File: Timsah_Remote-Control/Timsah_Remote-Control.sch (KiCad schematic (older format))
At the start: 41 parts, among them J1 Güç Girişi, J2 ICSP, J3 Klemens, SW1 Oto Depth, SW10 Backward, SW2 Lights, SW3 Up, SW4 Down, SW5 Power, SW6 Turn Back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

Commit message: Remote control board recreated.
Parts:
- added D2: LED, LED_THT:LED_D5.0mm, symbol Device:LED
- added R18: 1k, Resistor_THT:R_Axial_DIN0207_L6.3mm_D2.5mm_P10.16mm_Horizontal, symbol Device:R
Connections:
- net +5V: now also R4.1
- net Down: now also U3.10 (RE2/CCP5/AN7); no longer U3.28 (RD5/P1B/AN25)
- net ENABLE: now also U3.36 (AN9/C12IN2-/CTED2/CCP2/RB3); no longer U3.2 (AN0/C12IN0-/RA0)
- net Forward: now also U3.23 (RC4/SDA1/SDI1/AN16); no longer U3.19 (RD0/SCL2/SCK2/AN20)
- net GND: now also R18.1; no longer R4.1
- net OTO_DEPTH: now also U3.4 (DACOUT/VREF-/AN2/C2IN+/RA2); no longer U3.30 (RD7/RX2/DT2/P1D/AN27)
- net Right: now also U3.24 (RC5/SDO1/AN17); no longer U3.20 (RD1/SDI1/SDA2/CCP4/AN21)
- net SERVO_Cam: now also U3.20 (RD1/SDI1/SDA2/CCP4/AN21); no longer U3.17 (RC2/CTPLS/CCP1/P1A/T5CKI/AN14)
- net SERVO_Grip: now also U3.35 (AN8/CTED1/INT2/RB2); no longer U3.18 (RC3/SCL1/SCK1/AN15)
- net TURN_BACK: now also U3.18 (RC3/SCL1/SCK1/AN15); no longer U3.29 (RD6/TX2/CK2/P1C/AN26)
- net Up: now also U3.9 (RE1/P3B/AN6); no longer U3.27 (RD4/P2D/SDO2/AN24)
- net VRX-A: now also U3.15 (RC0/P2B/SOSCO/T1CKI/T3CKI/T3G); no longer U3.33 (AN12/SRI/FLT0/INT0/RB0)
- net VRX-B: now also U3.37 (AN11/T5G/IOC/RB4); no longer U3.35 (AN8/CTED1/INT2/RB2)
- net VRY-A: now also U3.16 (RC1/SOSCI/P2A/CCP2); no longer U3.34 (AN10/C12IN3-/INT1/RB1)
- net VRY-B: now also U3.38 (AN13/CCP3/T1G/IOC/CCP3/RB5); no longer U3.36 (AN9/C12IN2-/CTED2/CCP2/RB3)
- new net: D2.1 (K), R18.2
- new net LED: D2.2 (A), U3.17 (RC2/CTPLS/CCP1/P1A/T5CKI/AN14)
- no-connect marks 18 -> 17
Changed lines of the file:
@@
 Wire Wire Line
 	6950 950  6950 1050
-Text GLabel 1300 2650 0    50   Input ~ 0
+Text GLabel 1300 1650 0    50   Input ~ 0
 SERVO_Cam
 Text Notes 7000 2100 0    79   ~ 16
@@
 Wire Notes Line
 	6650 500  8350 500
-Text GLabel 4200 2450 2    50   Input ~ 0
+Text GLabel 1300 2450 0    50   Input ~ 0
 VRX-A
-Text GLabel 4200 2550 2    50   Input ~ 0
+Text GLabel 1300 2550 0    50   Input ~ 0
 VRY-A
-Text GLabel 4200 2650 2    50   Input ~ 0
+Text GLabel 4200 2850 2    50   Input ~ 0
 VRX-B
-Text GLabel 4200 2750 2    50   Input ~ 0
+Text GLabel 4200 2950 2    50   Input ~ 0
 VRY-B
 Wire Wire Line
-	4200 2450 4100 2450
-Wire Wire Line
-	4200 2550 4100 2550
-Wire Wire Line
 	4200 2650 4100 2650
-Wire Wire Line
-	4200 2750 4100 2750
 Wire Wire Line
 	1300 2650 1400 2650
@@
 Wire Wire Line
 	9100 4950 9350 4950
-$Comp
-L power:GND #PWR018
-U 1 1 5CC0738A
-P 9100 4350
-F 0 "#PWR018" H 9100 4100 50  0001 C CNN
-F 1 "GND" H 9105 4177 50  0000 C CNN
-F 2 "" H 9100 4350 50  0001 C CNN
-F 3 "" H 9100 4350 50  0001 C CNN
-	1    9100 4350
-	-1   0    0    1
-$EndComp
 Wire Wire Line
 	9100 4350 9100 4450
@@
 Wire Wire Line
 	1400 3050 1300 3050
-Text GLabel 4200 1750 2    50   Input ~ 0
+Text GLabel 4200 2750 2    50   Input ~ 0
 ENABLE
-Wire Wire Line
-	4200 1750 4100 1750
 Wire Wire Line
 	4200 1850 4100 1850
@@
 NoConn ~ 6800 2800
 NoConn ~ 1400 1150
-NoConn ~ 1400 1250
-NoConn ~ 1400 1350
-NoConn ~ 1400 2450
-NoConn ~ 1400 2550
-NoConn ~ 1400 2850
-NoConn ~ 1400 2950
-NoConn ~ 4100 2950
-NoConn ~ 4100 2850
 NoConn ~ 4100 2250
 NoConn ~ 4100 2150
 NoConn ~ 4100 2050
-NoConn ~ 4100 1950
 NoConn ~ 4100 1450
 NoConn ~ 4100 1350
@@
 Text Notes 3250 6800 0    50   ~ 10
 Yön Kontrolü:\n15 derece sağ veya sola dönme\n1 saniye ileri veya geri gitme
-Text GLabel 1300 1950 0    50   Input ~ 0
+Text GLabel 1300 1250 0    50   Input ~ 0
 Up
-Text GLabel 1300 2050 0    50   Input ~ 0
+Text GLabel 1300 1350 0    50   Input ~ 0
 Down
-Text GLabel 1300 2250 0    50   Input ~ 0
+Text GLabel 4200 1950 2    50   Input ~ 0
 OTO_DEPTH
-Text GLabel 1300 2150 0    50   Input ~ 0
+Text GLabel 1300 2750 0    50   Input ~ 0
 TURN_BACK
-Text GLabel 1300 1550 0    50   Input ~ 0
+Text GLabel 1300 2850 0    50   Input ~ 0
 Forward
-Text GLabel 1300 1650 0    50   Input ~ 0
+Text GLabel 1300 2950 0    50   Input ~ 0
 Right
 Text GLabel 1300 1750 0    50   Input ~ 0
@@
 Backward
 Wire Wire Line
-	1300 1550 1400 1550
-Wire Wire Line
 	1400 1650 1300 1650
 Wire Wire Line
@@
 Wire Wire Line
 	1400 1850 1300 1850
-Wire Wire Line
-	1300 1950 1400 1950
-Wire Wire Line
-	1400 2050 1300 2050
-Wire Wire Line
-	1300 2150 1400 2150
-Wire Wire Line
-	1400 2250 1300 2250
 Wire Wire Line
 	4100 1150 4200 1150
@@
 Wire Wire Line
 	7750 950  7750 1050
-Text GLabel 1300 2750 0    50   Input ~ 0
+Text GLabel 4200 2650 2    50   Input ~ 0
 SERVO_Grip
 Wire Wire Line
@@
 	1    0    0    -1
 $EndComp
+$Comp
+L Device:LED D2
+U 1 1 5D50D731
+P 5950 6000
+F 0 "D2" H 5950 5900 50  0000 C CNN
+F 1 "LED" H 5950 6100 50  0000 C CNN
+F 2 "LED_THT:LED_D5.0mm" H 5950 6000 50  0001 C CNN
+F 3 "~" H 5950 6000 50  0001 C CNN
+	1    5950 6000
+	-1   0    0    -1
+$EndComp
+$Comp
+L Device:R R18
+U 1 1 5D50E94F
+P 6350 6000
+F 0 "R18" V 6250 6000 50  0000 C CNN
+F 1 "1k" V 6350 6000 50  0000 C CNN
+F 2 "Resistor_THT:R_Axial_DIN0207_L6.3mm_D2.5mm_P10.16mm_Horizontal" V 6280 6000 50  0001 C CNN
+F 3 "~" H 6350 6000 50  0001 C CNN
+	1    6350 6000
+	0    1    -1   0
+$EndComp
+Wire Wire Line
+	6200 6000 6100 6000
+$Comp
+L power:GND #PWR0103
+U 1 1 5D5228AB
+P 6600 6000
+F 0 "#PWR0103" H 6600 5750 50  0001 C CNN
+F 1 "GND" H 6605 5827 50  0000 C CNN
+F 2 "" H 6600 6000 50  0001 C CNN
+F 3 "" H 6600 6000 50  0001 C CNN
+	1    6600 6000
+	0    -1   1    0
+$EndComp
+Wire Wire Line
+	6600 6000 6500 6000
+Wire Wire Line
+	1300 2850 1400 2850
+Wire Wire Line
+	1400 2950 1300 2950
+Wire Wire Line
+	1300 2450 1400 2450
+Text GLabel 1300 2650 0    50   Input ~ 0
+LED
+Wire Wire Line
+	1300 2550 1400 2550
+Text GLabel 5650 6000 0    50   Input ~ 0
+LED
+Wire Wire Line
+	5650 6000 5800 6000
+Wire Wire Line
+	4200 2850 4100 2850
+Wire Wire Line
+	4100 2950 4200 2950
+Wire Wire Line
+	4200 1950 4100 1950
+NoConn ~ 1400 2250
+NoConn ~ 1400 2150
+NoConn ~ 1400 2050
+NoConn ~ 1400 1950
+NoConn ~ 1400 1550
+Wire Wire Line
+	1300 1350 1400 1350
+Wire Wire Line
+	1400 1250 1300 1250
+NoConn ~ 4100 2450
+NoConn ~ 4100 2550
+Wire Wire Line
+	4200 2750 4100 2750
+NoConn ~ 4100 1750
+$Comp
+L power:+5V #PWR?
+U 1 1 5D6E4C63
+P 9100 4350
+F 0 "#PWR?" H 9100 4200 50  0001 C CNN
+F 1 "+5V" H 9115 4523 50  0000 C CNN
+F 2 "" H 9100 4350 50  0001 C CNN
+F 3 "" H 9100 4350 50  0001 C CNN
+	1    9100 4350
+	1    0    0    -1
+$EndComp

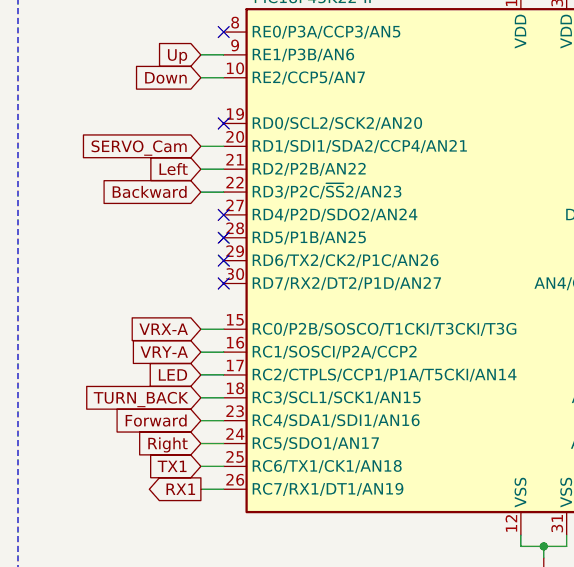
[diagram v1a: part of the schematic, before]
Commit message: Remote controller joystick pins changed.
Joystick A pins do not connected to analog pins.
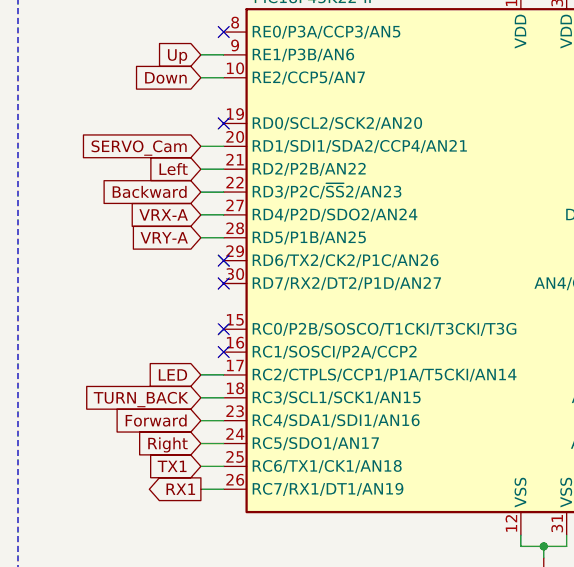
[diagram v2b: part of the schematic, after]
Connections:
- net VRX-A: now also U3.27 (RD4/P2D/SDO2/AN24); no longer U3.15 (RC0/P2B/SOSCO/T1CKI/T3CKI/T3G)
- net VRY-A: now also U3.28 (RD5/P1B/AN25); no longer U3.16 (RC1/SOSCI/P2A/CCP2)
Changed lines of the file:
@@
 Wire Notes Line
 	6650 500  8350 500
-Text GLabel 1300 2450 0    50   Input ~ 0
+Text GLabel 1300 1950 0    50   Input ~ 0
 VRX-A
-Text GLabel 1300 2550 0    50   Input ~ 0
+Text GLabel 1300 2050 0    50   Input ~ 0
 VRY-A
 Text GLabel 4200 2850 2    50   Input ~ 0
@@
 Wire Wire Line
 	1400 2950 1300 2950
-Wire Wire Line
-	1300 2450 1400 2450
 Text GLabel 1300 2650 0    50   Input ~ 0
 LED
-Wire Wire Line
-	1300 2550 1400 2550
 Text GLabel 5650 6000 0    50   Input ~ 0
 LED
@@
 NoConn ~ 1400 2250
 NoConn ~ 1400 2150
-NoConn ~ 1400 2050
-NoConn ~ 1400 1950
 NoConn ~ 1400 1550
 Wire Wire Line
@@
 	1    0    0    -1
 $EndComp
+Wire Wire Line
+	1300 2050 1400 2050
+Wire Wire Line
+	1400 1950 1300 1950
+NoConn ~ 1400 2450
+NoConn ~ 1400 2550
 $EndSCHEMATC

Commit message: Hardware Update
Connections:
- net +5V: no longer R4.1
- net GND: now also R4.1
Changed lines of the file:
@@
 	4200 2750 4100 2750
 NoConn ~ 4100 1750
-$Comp
-L power:+5V #PWR?
-U 1 1 5D6E4C63
-P 9100 4350
-F 0 "#PWR?" H 9100 4200 50  0001 C CNN
-F 1 "+5V" H 9115 4523 50  0000 C CNN
-F 2 "" H 9100 4350 50  0001 C CNN
-F 3 "" H 9100 4350 50  0001 C CNN
-	1    9100 4350
-	1    0    0    -1
-$EndComp
 Wire Wire Line
 	1300 2050 1400 2050
@@
 NoConn ~ 1400 2450
 NoConn ~ 1400 2550
+$Comp
+L power:GND #PWR?
+U 1 1 5D52181D
+P 9100 4350
+F 0 "#PWR?" H 9100 4100 50  0001 C CNN
+F 1 "GND" H 9105 4177 50  0000 C CNN
+F 2 "" H 9100 4350 50  0001 C CNN
+F 3 "" H 9100 4350 50  0001 C CNN
+	1    9100 4350
+	-1   0    0    1
+$EndComp
 $EndSCHEMATC
